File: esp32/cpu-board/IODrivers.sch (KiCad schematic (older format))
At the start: 11 parts, among them J3 Conn_01x10, J4 Conn_01x10, Q1 PMBTA42DS,125, Q2 PMBTA42DS,125, Q3 PMBTA42DS,125, Q4 PMBTA42DS,125, Q5 PMBTA42DS,125, U4 MAX7320

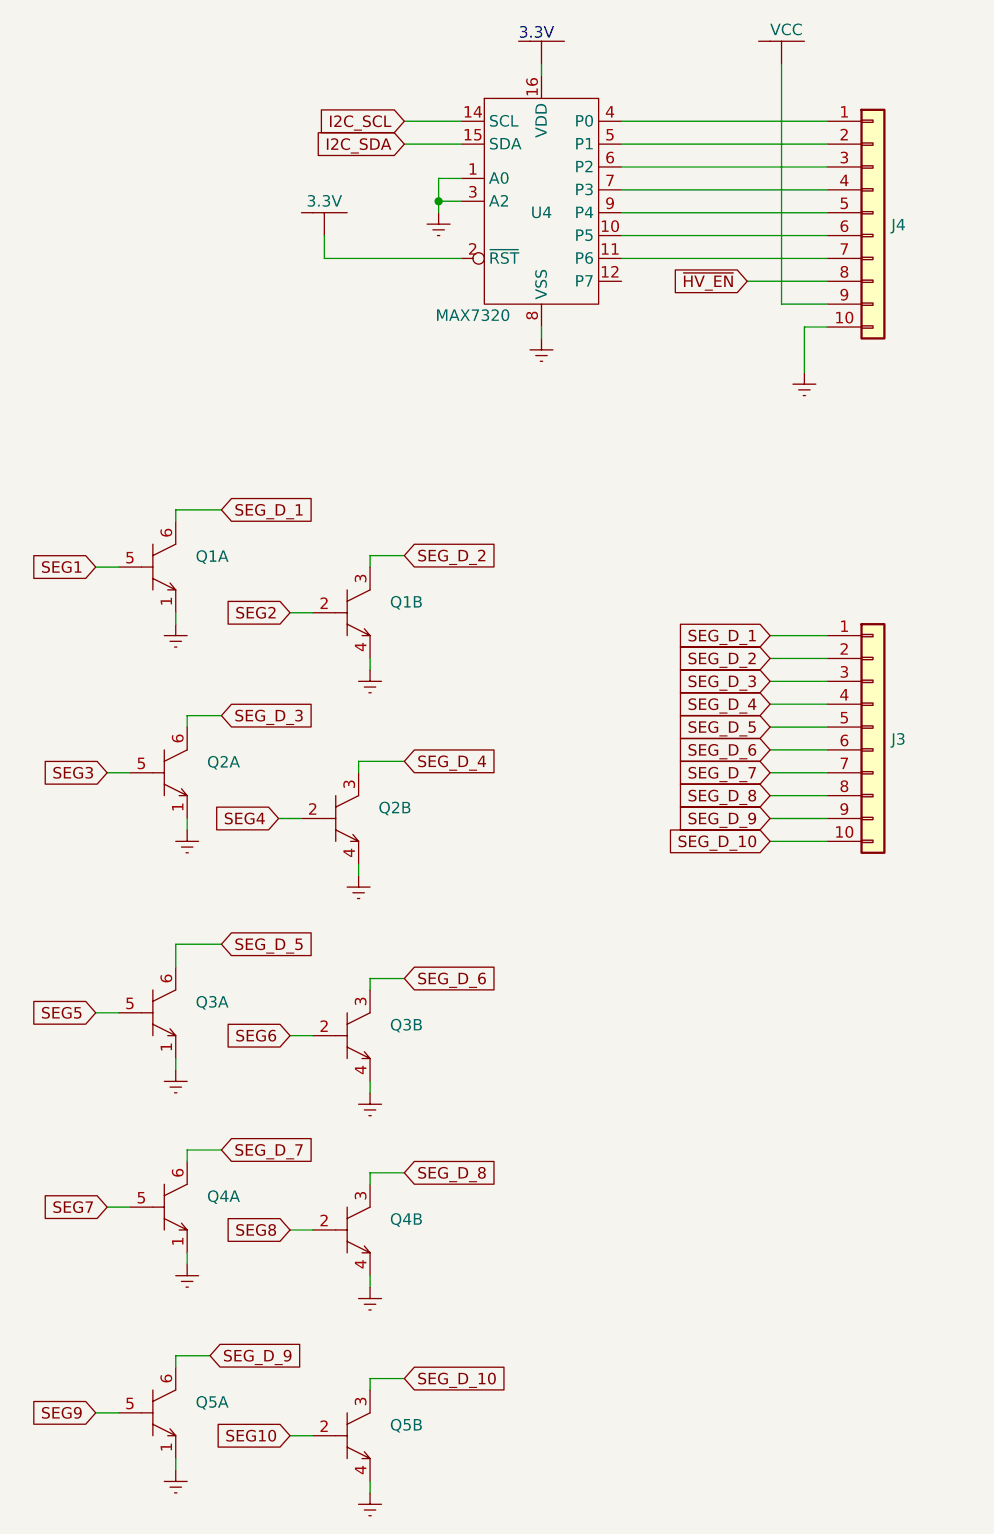
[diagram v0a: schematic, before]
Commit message: First attempt at ensuring proper grounding Added capacitor to the reset pin Extended the reset line to the IO extenders
[git-p4: depot-paths = "//depot/nixiestat/": change = 324]
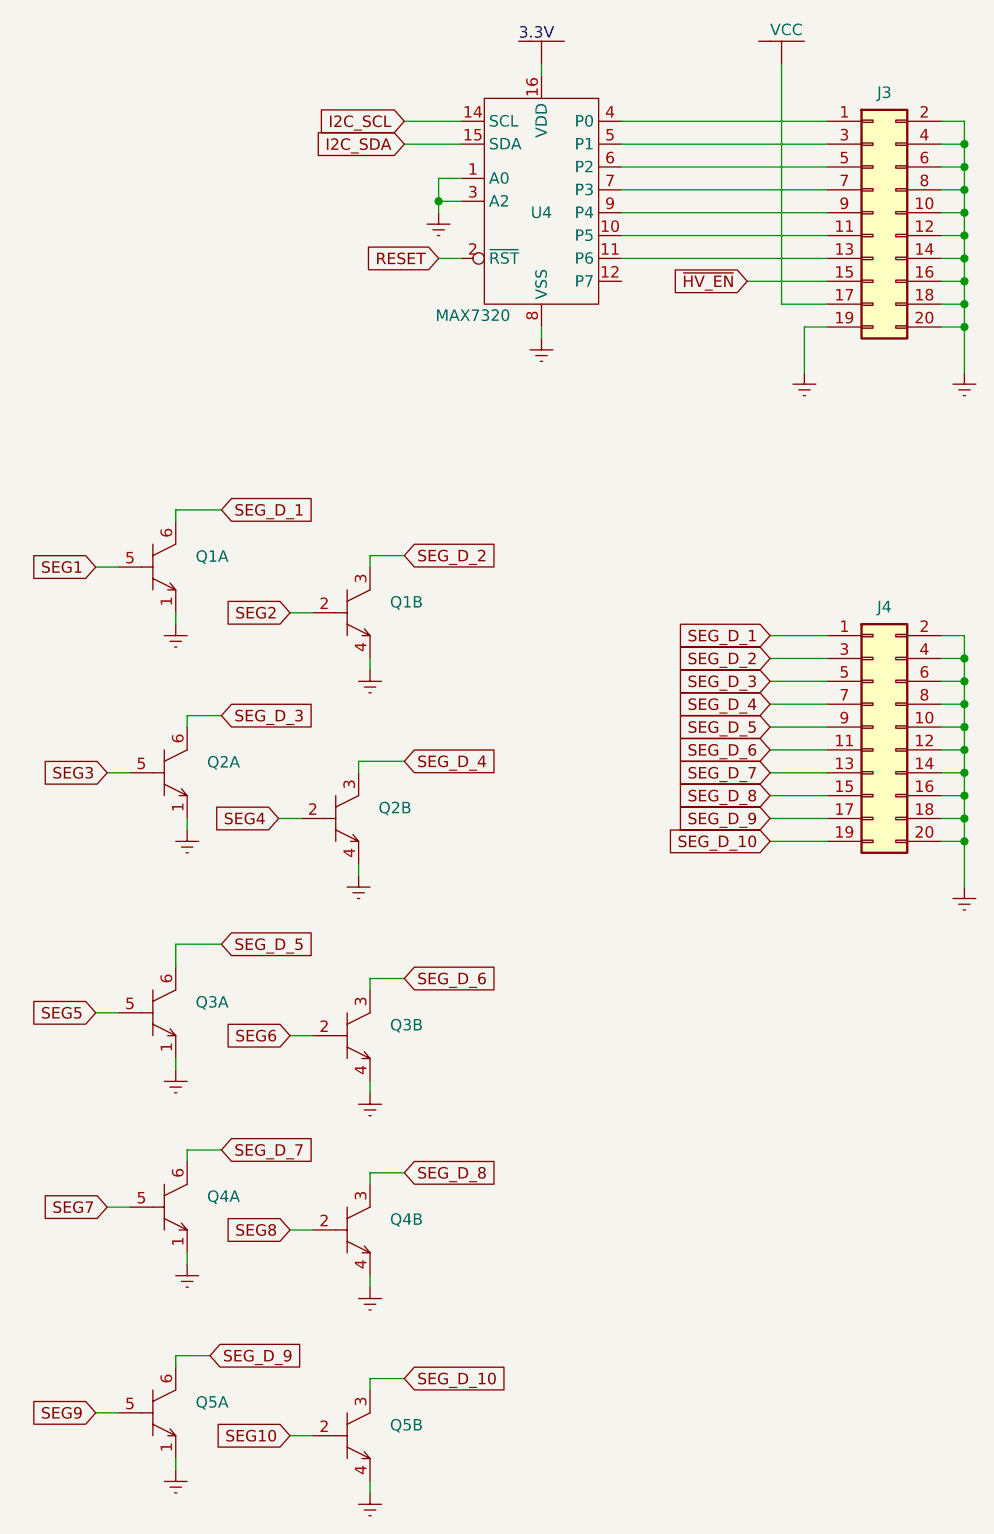
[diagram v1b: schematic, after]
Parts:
- removed J3, J4: Conn_01x10, croftj:Mill-Max-295x10, symbol Connector_Generic:Conn_01x10
- removed V11: 3.3V, symbol croftj:3.3V
- added J3: Conn_02x10_Odd_Even, croftj:pcb_jack-2x10, symbol Connector_Generic:Conn_02x10_Odd_Even
- added J4: Conn_02x10_Odd_Even, croftj:pcb_jack-2x10-mirror, symbol Connector_Generic:Conn_02x10_Odd_Even
- gave numbers to parts that had none: 1
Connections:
- net +3.3V: no longer U4.2 (~RST~)
- net GNDREF: now also J3.10 (Pin_10), J3.12 (Pin_12), J3.14 (Pin_14), J3.16 (Pin_16), J3.18 (Pin_18), J3.19 (Pin_19), J3.2 (Pin_2), J3.20 (Pin_20), J3.4 (Pin_4), J3.6 (Pin_6), J3.8 (Pin_8), J4.10 (Pin_10), J4.12 (Pin_12), J4.14 (Pin_14), J4.16 (Pin_16), J4.18 (Pin_18), J4.2 (Pin_2), J4.20 (Pin_20), J4.4 (Pin_4), J4.6 (Pin_6), J4.8 (Pin_8)
- net SEG_D_1: now also J4.1 (Pin_1)
- net SEG_D_10: now also J4.19 (Pin_19)
- net SEG_D_2: now also J4.3 (Pin_3)
- net SEG_D_3: now also J4.5 (Pin_5)
- net SEG_D_4: now also J4.7 (Pin_7)
- net SEG_D_5: now also J4.9 (Pin_9)
- net SEG_D_6: now also J4.11 (Pin_11)
- net SEG_D_7: now also J4.13 (Pin_13)
- net SEG_D_8: now also J4.15 (Pin_15)
- net SEG_D_9: now also J4.17 (Pin_17)
- net VCC: now also J3.17 (Pin_17)
- net ~HV_EN~: now also J3.15 (Pin_15)
- net at U4.4 (P0): now also J3.1 (Pin_1)
- net at U4.5 (P1): now also J3.3 (Pin_3)
- net at U4.6 (P2): now also J3.5 (Pin_5)
- net at U4.7 (P3): now also J3.7 (Pin_7)
- net at U4.9 (P4): now also J3.9 (Pin_9)
- net at U4.10 (P5): now also J3.11 (Pin_11)
- net at U4.11 (P6): now also J3.13 (Pin_13)
- new net RESET: U4.2 (~RST~)
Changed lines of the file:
@@
-$EndComp
-$Comp
-L Connector_Generic:Conn_01x10 J4
-U 1 1 623C0B29
-P 6050 1600
-F 0 "J4" H 6130 1546 50  0000 L CNN
-F 1 "Conn_01x10" H 6130 1501 50  0001 L CNN
-F 2 "croftj:Mill-Max-295x10" H 6050 1600 50  0001 C CNN
-F 3 "~" H 6050 1600 50  0001 C CNN
-	1    6050 1600
-	1    0    0    -1
 $EndComp
 $Comp
@@
 Text GLabel 5600 4350 0    50   Input ~ 0
 SEG_D_10
-$Comp
-L Connector_Generic:Conn_01x10 J?
-U 1 1 6238B509
-P 6050 3850
-AR Path="/6238B509" Ref="J?"  Part="1"
-AR Path="/62313FED/6238B509" Ref="J3"  Part="1"
-F 0 "J3" H 6130 3796 50  0000 L CNN
-F 1 "Conn_01x10" H 6130 3751 50  0001 L CNN
-F 2 "croftj:Mill-Max-295x10" H 6050 3850 50  0001 C CNN
-F 3 "~" H 6050 3850 50  0001 C CNN
-	1    6050 3850
-	1    0    0    -1
-$EndComp
 Wire Wire Line
 	5600 3450 5850 3450
@@
 	5650 2000 5850 2000
 $Comp
-L croftj:3.3V V?
-U 1 1 6255DC63
-P 3650 1550
-AR Path="/6255DC63" Ref="V?"  Part="1"
-AR Path="/62313FED/6255DC63" Ref="V11"  Part="1"
-F 0 "V11" H 3600 1450 50  0001 C CNN
-F 1 "3.3V" H 3650 1550 50  0000 C CNN
-F 2 "" H 3650 1550 50  0001 C CNN
-F 3 "" H 3650 1550 50  0001 C CNN
-	1    3650 1550
-	1    0    0    -1
-$EndComp
-Wire Wire Line
-	3650 1800 4250 1800
-Wire Wire Line
-	3650 1700 3650 1800
-$Comp
-L croftj:VCC V?
+L croftj:VCC V14
 U 1 1 61E55107
 P 5650 800
-F 0 "V?" H 5550 700 50  0001 C CNN
+F 0 "V14" H 5550 700 50  0001 C CNN
 F 1 "VCC" H 5600 800 50  0000 L CNN
 F 2 "" H 5500 850 50  0001 C CNN
@@
 	1    0    0    -1
 $EndComp
+Text GLabel 4150 1800 0    50   Input ~ 0
+RESET
+Wire Wire Line
+	4150 1800 4250 1800
+$Comp
+L Connector_Generic:Conn_02x10_Odd_Even J3
+U 1 1 623DCFF5
+P 6050 1600
+F 0 "J3" H 6100 2125 50  0000 C CNN
+F 1 "Conn_02x10_Odd_Even" H 6100 2126 50  0001 C CNN
+F 2 "croftj:pcb_jack-2x10" H 6050 1600 50  0001 C CNN
+F 3 "~" H 6050 1600 50  0001 C CNN
+	1    6050 1600
+	1    0    0    -1
+$EndComp
+$Comp
+L power:GNDREF #PWR?
+U 1 1 623DF10F
+P 6450 2300
+AR Path="/623DF10F" Ref="#PWR?"  Part="1"
+AR Path="/62313FED/623DF10F" Ref="#PWR0122"  Part="1"
+F 0 "#PWR0122" H 6450 2050 50  0001 C CNN
+F 1 "GNDREF" H 6455 2127 50  0001 C CNN
+F 2 "" H 6450 2300 50  0001 C CNN
+F 3 "" H 6450 2300 50  0001 C CNN
+	1    6450 2300
+	-1   0    0    -1
+$EndComp
+Wire Wire Line
+	6450 2100 6450 2300
+Wire Wire Line
+	6350 2100 6450 2100
+Wire Wire Line
+	6450 2100 6450 2000
+Wire Wire Line
+	6450 2000 6350 2000
+Connection ~ 6450 2100
+Wire Wire Line
+	6450 2000 6450 1900
+Wire Wire Line
+	6450 1900 6350 1900
+Wire Wire Line
+	6450 1900 6450 1800
+Wire Wire Line
+	6450 1800 6350 1800
+Wire Wire Line
+	6450 1800 6450 1700
+Wire Wire Line
+	6450 1700 6350 1700
+Wire Wire Line
+	6450 1700 6450 1600
+Wire Wire Line
+	6450 1600 6350 1600
+Wire Wire Line
+	6450 1600 6450 1500
+Wire Wire Line
+	6450 1500 6350 1500
+Wire Wire Line
+	6450 1500 6450 1400
+Wire Wire Line
+	6450 1400 6350 1400
+Wire Wire Line
+	6450 1400 6450 1300
+Wire Wire Line
+	6450 1300 6350 1300
+Wire Wire Line
+	6450 1300 6450 1200
+Wire Wire Line
+	6450 1200 6350 1200
+Connection ~ 6450 1300
+Connection ~ 6450 1400
+Connection ~ 6450 1500
+Connection ~ 6450 1600
+Connection ~ 6450 1700
+Connection ~ 6450 1800
+Connection ~ 6450 1900
+Connection ~ 6450 2000
+$Comp
+L Connector_Generic:Conn_02x10_Odd_Even J4
+U 1 1 623F7AD0
+P 6050 3850
+F 0 "J4" H 6100 4375 50  0000 C CNN
+F 1 "Conn_02x10_Odd_Even" H 6100 4376 50  0001 C CNN
+F 2 "croftj:pcb_jack-2x10-mirror" H 6050 3850 50  0001 C CNN
+F 3 "~" H 6050 3850 50  0001 C CNN
+	1    6050 3850
+	1    0    0    -1
+$EndComp
+$Comp
+L power:GNDREF #PWR?
+U 1 1 623F7AD6
+P 6450 4550
+AR Path="/623F7AD6" Ref="#PWR?"  Part="1"
+AR Path="/62313FED/623F7AD6" Ref="#PWR0123"  Part="1"
+F 0 "#PWR0123" H 6450 4300 50  0001 C CNN
+F 1 "GNDREF" H 6455 4377 50  0001 C CNN
+F 2 "" H 6450 4550 50  0001 C CNN
+F 3 "" H 6450 4550 50  0001 C CNN
+	1    6450 4550
+	-1   0    0    -1
+$EndComp
+Wire Wire Line
+	6450 4350 6450 4550
+Wire Wire Line
+	6350 4350 6450 4350
+Wire Wire Line
+	6450 4350 6450 4250
+Wire Wire Line
+	6450 4250 6350 4250
+Connection ~ 6450 4350
+Wire Wire Line
+	6450 4250 6450 4150
+Wire Wire Line
+	6450 4150 6350 4150
+Wire Wire Line
+	6450 4150 6450 4050
+Wire Wire Line
+	6450 4050 6350 4050
+Wire Wire Line
+	6450 4050 6450 3950
+Wire Wire Line
+	6450 3950 6350 3950
+Wire Wire Line
+	6450 3950 6450 3850
+Wire Wire Line
+	6450 3850 6350 3850
+Wire Wire Line
+	6450 3850 6450 3750
+Wire Wire Line
+	6450 3750 6350 3750
+Wire Wire Line
+	6450 3750 6450 3650
+Wire Wire Line
+	6450 3650 6350 3650
+Wire Wire Line
+	6450 3650 6450 3550
+Wire Wire Line
+	6450 3550 6350 3550
+Wire Wire Line
+	6450 3550 6450 3450
+Wire Wire Line
+	6450 3450 6350 3450
+Connection ~ 6450 3550
+Connection ~ 6450 3650
+Connection ~ 6450 3750
+Connection ~ 6450 3850
+Connection ~ 6450 3950
+Connection ~ 6450 4050
+Connection ~ 6450 4150
+Connection ~ 6450 4250
 $EndSCHEMATC
